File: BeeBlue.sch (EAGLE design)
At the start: 3 parts, among them U1 HC_05

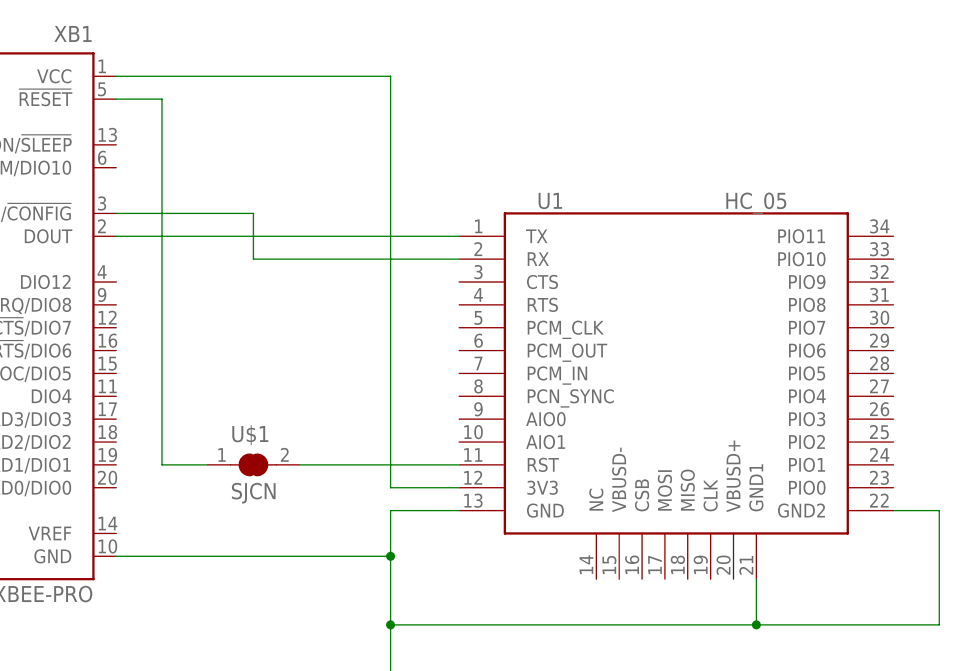
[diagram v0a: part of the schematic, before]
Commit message: Added jumper for setting command mode
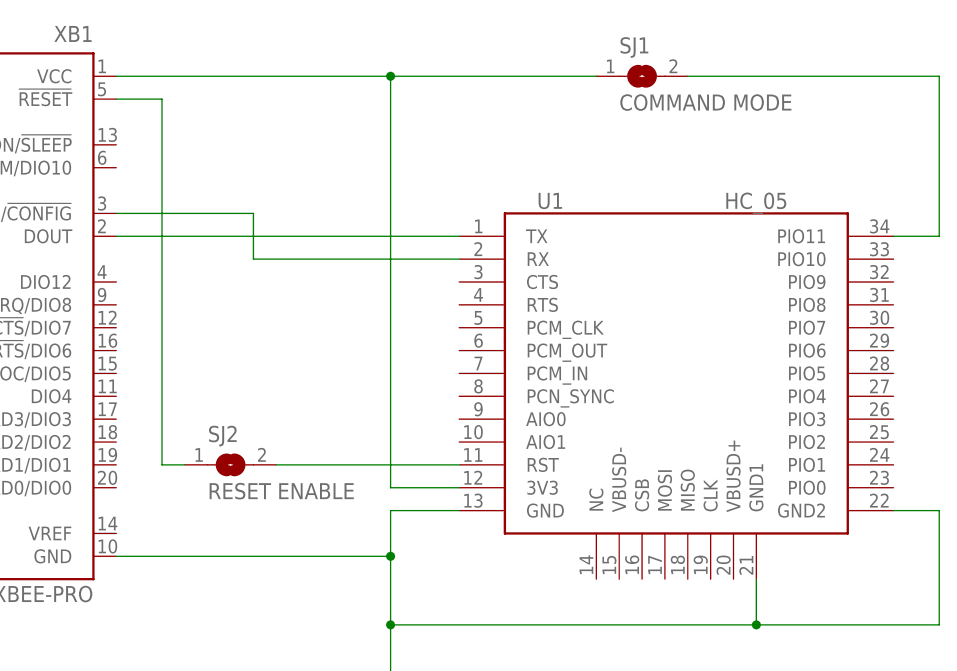
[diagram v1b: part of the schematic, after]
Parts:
- removed U$1: SJCN, freetronics-jon:SJCN
- added SJ1: COMMAND MODE, freetronics-jon:SJN
- added SJ2: RESET ENABLE, freetronics-jon:SJN
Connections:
- new net N$1: SJ1.2, U1.PIO11
- net N$4: now also SJ1.1
- net N$5: now also SJ2.2; no longer U$1.2
- net N$6: now also SJ2.1; no longer U$1.1
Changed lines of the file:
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@@
 <part name="XB1" library="freetronics-jon" deviceset="XBEE" device="-PRO"/>
 <part name="U1" library="freetronics-jon" deviceset="HC_05" device=""/>
-<part name="U$1" library="freetronics-jon" deviceset="SJC" device="N"/>
+<part name="SJ2" library="freetronics-jon" deviceset="SJ" device="N" value="RESET ENABLE"/>
+<part name="SJ1" library="freetronics-jon" deviceset="SJ" device="N" value="COMMAND MODE"/>
 </parts>
 <sheets>
@@
 <instance part="XB1" gate="G$1" x="66.04" y="116.84" rot="MR0"/>
 <instance part="U1" gate="G$1" x="142.24" y="109.22"/>
-<instance part="U$1" gate="G$1" x="96.52" y="99.06"/>
+<instance part="SJ2" gate="1" x="93.98" y="99.06"/>
+<instance part="SJ1" gate="1" x="139.7" y="142.24"/>
 </instances>
 <busses>
@@
 <pinref part="XB1" gate="G$1" pin="VCC"/>
 <wire x1="111.76" y1="142.24" x2="81.28" y2="142.24" width="0.1524" layer="91"/>
+<pinref part="SJ1" gate="1" pin="1"/>
+<wire x1="111.76" y1="142.24" x2="134.62" y2="142.24" width="0.1524" layer="91"/>
+<junction x="111.76" y="142.24"/>
 </segment>
 </net>
 <net name="N$5" class="0">
 <segment>
-<pinref part="U$1" gate="G$1" pin="2"/>
+<pinref part="SJ2" gate="1" pin="2"/>
 <pinref part="U1" gate="G$1" pin="RST"/>
-<wire x1="101.6" y1="99.06" x2="119.38" y2="99.06" width="0.1524" layer="91"/>
+<wire x1="99.06" y1="99.06" x2="119.38" y2="99.06" width="0.1524" layer="91"/>
 </segment>
 </net>
 <net name="N$6" class="0">
 <segment>
-<pinref part="U$1" gate="G$1" pin="1"/>
-<wire x1="91.44" y1="99.06" x2="86.36" y2="99.06" width="0.1524" layer="91"/>
+<pinref part="SJ2" gate="1" pin="1"/>
+<wire x1="88.9" y1="99.06" x2="86.36" y2="99.06" width="0.1524" layer="91"/>
 <wire x1="86.36" y1="99.06" x2="86.36" y2="139.7" width="0.1524" layer="91"/>
 <pinref part="XB1" gate="G$1" pin="!RESET"/>
@@
 </segment>
 </net>
+<net name="N$1" class="0">
+<segment>
+<pinref part="SJ1" gate="1" pin="2"/>
+<wire x1="144.78" y1="142.24" x2="172.72" y2="142.24" width="0.1524" layer="91"/>
+<wire x1="172.72" y1="142.24" x2="172.72" y2="124.46" width="0.1524" layer="91"/>
+<pinref part="U1" gate="G$1" pin="PIO11"/>
+<wire x1="172.72" y1="124.46" x2="167.64" y2="124.46" width="0.1524" layer="91"/>
+</segment>
+</net>
